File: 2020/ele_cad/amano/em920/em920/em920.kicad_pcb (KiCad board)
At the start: 2 copper layers, 45.7 x 63.5 mm, 4 parts, among them J1 Conn_01x06, U1 ATtiny85-20PU, U2 TY92SS

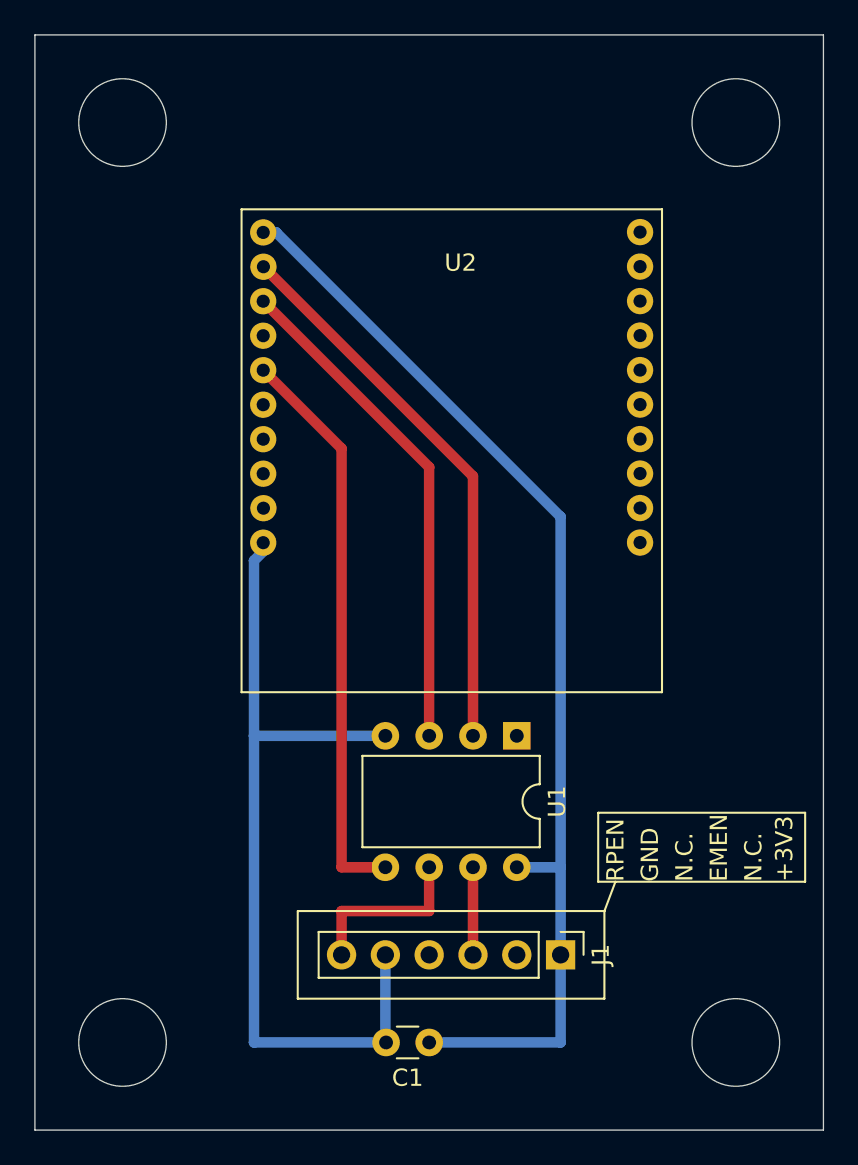
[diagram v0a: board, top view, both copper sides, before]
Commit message: em920のフォルダ構造を変更
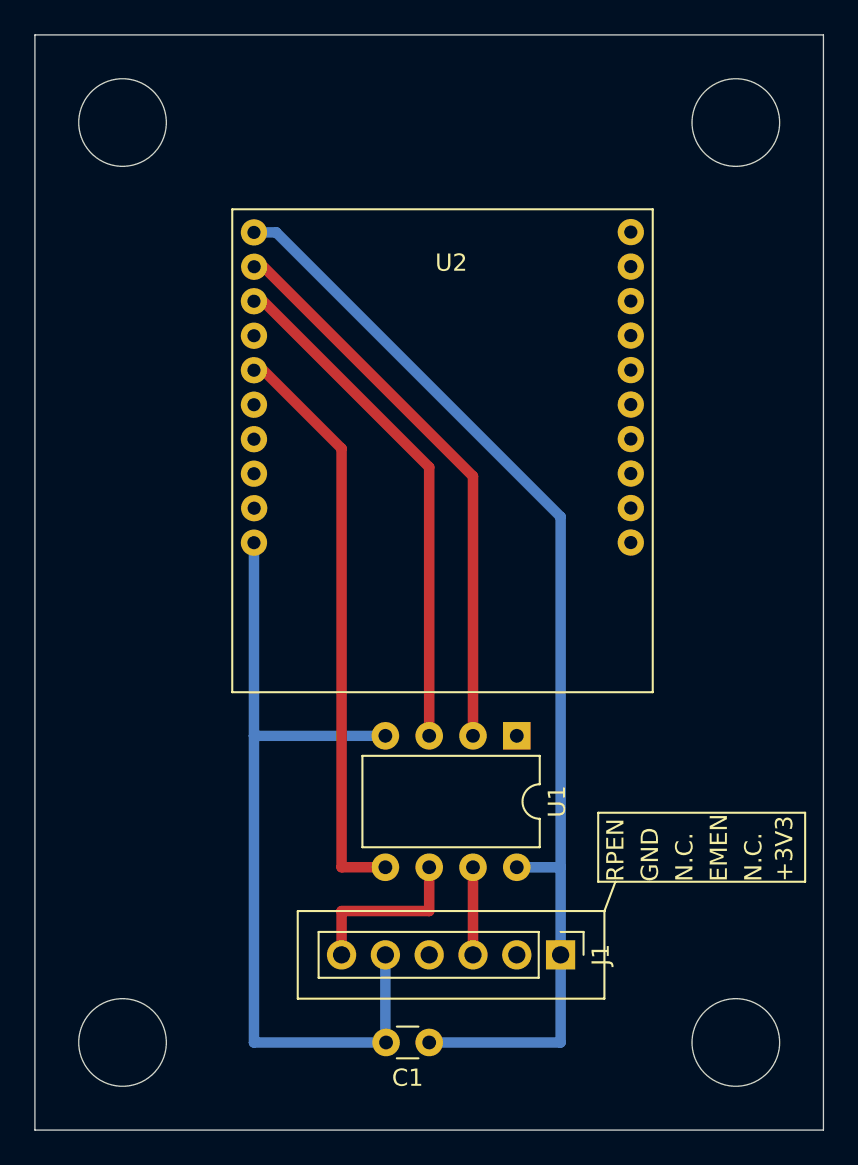
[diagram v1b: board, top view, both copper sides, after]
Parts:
- moved U2 0.54 mm to (64.8, 127.0)
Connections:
- J1 pad 2: (no net) -> Net-(J1-Pad2)
- J1 pad 4: (no net) -> Net-(J1-Pad4)
- U1 pad 1: (no net) -> Net-(U1-Pad1)
- U2 pad 12: (no net) -> Net-(U2-Pad12)
- U2 pad 13: (no net) -> Net-(U2-Pad13)
- U2 pad 16: (no net) -> Net-(U2-Pad16)
- U2 pad 9: (no net) -> Net-(U2-Pad9)
